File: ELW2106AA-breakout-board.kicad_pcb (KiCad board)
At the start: 2 copper layers, 77 x 18 mm, 28 parts, among them J1 Conn_02x04_Male-custom, U1 TLV61046ADB, U2 XC6206P332MR, U3 TXS0108EPW

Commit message: second revision
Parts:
- moved C10 11.6 mm to (117.9, 113.7), turned to 90 degrees
- moved L1 2.78 mm to (121.9, 103.2), turned to 0 degrees
- moved C4 1.86 mm to (137.4, 101.1), turned to 0 degrees
- moved R3 1.18 mm to (126.4, 101.2), turned to 180 degrees
- moved C7 0.92 mm to (140.9, 102.2), turned to -90 degrees
- moved R4 0.29 mm to (126.4, 103.7), turned to 0 degrees
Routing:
- net VCC: track 96.5 -> 55.1 mm, vias 2 -> 3
- net Net-(L1-Pad2): track 13.3 -> 5.12 mm
- net GND: track 13.8 -> 8.37 mm, vias 6 -> 33
- net +3V3: track 47.9 -> 43.7 mm
- net +16V: track 39.4 -> 42.8 mm, vias 2 -> 3
- net Net-(R3-Pad2): track 3.94 -> 5.46 mm
- net /OLED_CS: track 40.5 -> 41.7 mm
- net /OLED_RST: track 43.0 -> 44.1 mm
- net /OLED_D/C#: track 45.6 -> 46.6 mm
- net /OLED_SCLK: track 48.1 -> 49.0 mm
- net /OLED_MOSI: track 50.5 -> 51.3 mm
- added copper zone on B.Cu, net VCC

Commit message: third revision
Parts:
- C1, C10, C11, C12, C13, C2, C3, C4, C5, C6, C7, C8, C9, H1, J1, L1, R3, R4, TP1, TP2, TP3, TP4, TP5, TP6, TP7, U1, U2, U3: moved to F.Cu
- moved TP6 75.7 mm to (81.8, 102.0), turned to 0 degrees
- moved TP5 71.3 mm to (83.9, 102.0), turned to 0 degrees
- moved TP3 66.9 mm to (86.1, 102.0), turned to 0 degrees
- moved TP2 62.3 mm to (88.4, 102.0), turned to 0 degrees
- moved TP4 57.7 mm to (90.7, 102.0), turned to 0 degrees
- moved TP7 53.0 mm to (93.1, 102.0), turned to 0 degrees
- moved H1 47.9 mm to (95.6, 107.9)
- moved J1 47.5 mm to (143.3, 103.9), turned to 0 degrees
- moved TP1 43.3 mm to (97.9, 115.1), turned to 0 degrees
- moved C7 42.6 mm to (98.3, 102.2)
- moved C13 37.1 mm to (138.1, 102.9), turned to 0 degrees
- moved C6 36.4 mm to (101.4, 114.7), turned to 180 degrees
- moved C4 35.6 mm to (101.8, 101.0), turned to 180 degrees
- moved C1 31.9 mm to (103.6, 102.5), turned to 0 degrees
- moved C2 31.9 mm to (103.6, 103.9), turned to 0 degrees
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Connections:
- U3 pad 10: unconnected-(U3-Pad10) -> +3V3
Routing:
- net +3V3: track 43.7 -> 52.5 mm
- net GND: track 8.37 -> 7.89 mm, vias 33 -> 36
- added copper zone on F.Cu, net VCC
- removed copper zone on B.Cu, net VCC
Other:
- outline, holes or cut-outs redrawn
- board text added: "CS"
- board text added: "D/C"
- board text added: "ELW2106AA 4-wire SPI only"
- board text added: "GND"
- board text added: "MOSI"
- board text added: "RST"
- board text added: "SCLK"
- board text added: "VCC"

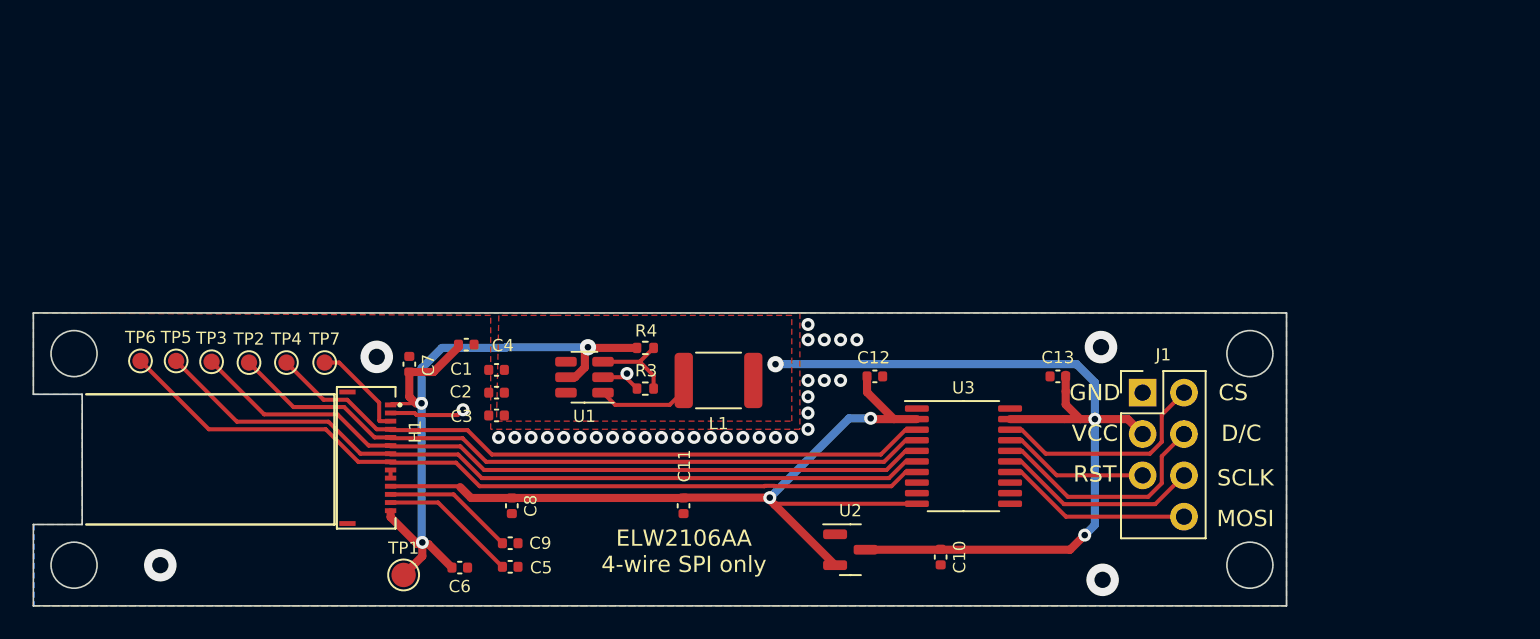
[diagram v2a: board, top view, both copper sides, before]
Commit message: replace TXS0108E with good ol' SN74LVC245
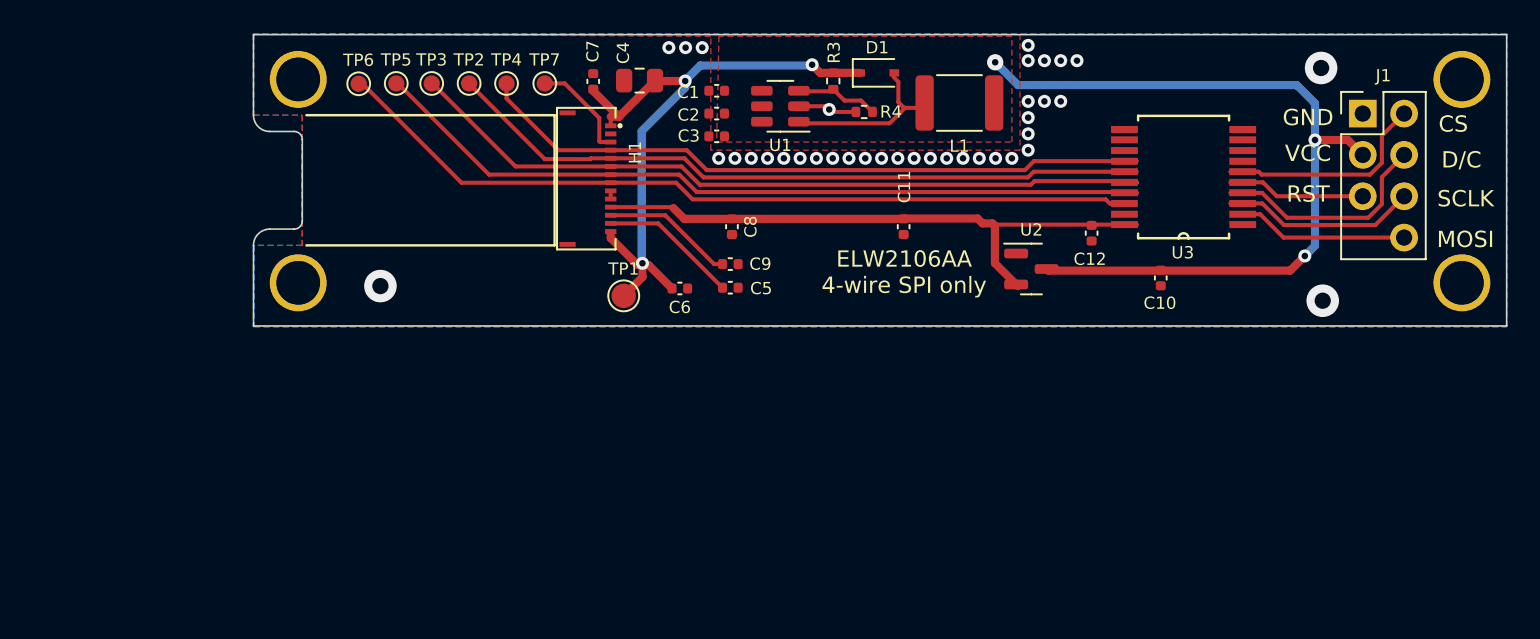
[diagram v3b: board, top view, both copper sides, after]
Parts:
- removed C13: 100nF, Capacitor_SMD:C_0402_1005Metric
- added D1: 1N5819WS, Diode_SMD:D_SOD-323, F.Cu at (127.0, 84.2)
- added MH1: MountingHole_Pad, custom:MountingHole_2.7mm_M2.5_Custom_Pad, B.Cu at (91.5, 97.2)
- added MH2: MountingHole_Pad, custom:MountingHole_2.7mm_M2.5_Custom_Pad, B.Cu at (91.5, 84.7)
- added MH3: MountingHole_Pad, custom:MountingHole_2.7mm_M2.5_Custom_Pad, B.Cu at (162.9, 97.2)
- added MH4: MountingHole_Pad, custom:MountingHole_2.7mm_M2.5_Custom_Pad, B.Cu at (162.9, 84.7)
- C10, C11: value 10uF -> 1µF
- C4: value 10µF -> 22µF; footprint Capacitor_SMD:C_0402_1005Metric -> Capacitor_SMD:C_0805_2012Metric
- C8, C9: value 1.0µF -> 1µF
- L1: value 12µH -> 22µH
- U1: value TLV61046ADB -> MT3608
- U3: value TXS0108EPW -> SN74LVC245ADBRG4; footprint Package_SO:TSSOP-20_4.4x6.5mm_P0.65mm -> SN74LVC245ADBRG4:SOP65P780X200-20N
- moved L1 22.6 mm to (132.1, 86.1)
- moved C6 21.8 mm to (114.9, 97.5)
- moved C9 21.8 mm to (118.0, 96.0)
- moved H1 21.8 mm to (109.2, 90.8)
- moved J1 21.8 mm to (156.9, 86.8)
- moved C11 21.8 mm to (128.7, 93.7)
- moved C5 21.8 mm to (118.0, 97.5)
- moved TP1 21.8 mm to (111.5, 98.0)
- moved TP2 21.8 mm to (102.0, 84.9)
- moved TP4 21.8 mm to (104.2, 84.9)
- moved U3 21.8 mm to (145.8, 90.7), turned to 180 degrees
- moved C1 21.8 mm to (117.2, 85.3)
- moved C2 21.8 mm to (117.2, 86.8)
- moved C10 21.8 mm to (144.4, 96.8)
- moved C3 21.8 mm to (117.2, 88.2)
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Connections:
- U1 pad 5: +16V -> VCC
- U1 pad 6: VCC -> unconnected-(U1-Pad6)
- U3 pad 1: unconnected-(U3-Pad1) -> GND
- U3 pad 10: +3V3 -> GND
- U3 pad 12: unconnected-(U3-Pad12) -> GND
- U3 pad 13: unconnected-(U3-Pad13) -> GND
- U3 pad 14: /MOSI -> /OLED_CS
- U3 pad 15: /SCLK -> /OLED_RST
- U3 pad 16: /D/C -> /OLED_D/C#
- U3 pad 17: /RESET -> /OLED_SCLK
- U3 pad 18: /CS -> /OLED_MOSI
- U3 pad 19: VCC -> GND
- U3 pad 2: +3V3 -> /MOSI
- U3 pad 20: unconnected-(U3-Pad20) -> +3V3
- U3 pad 3: /OLED_CS -> /SCLK
- U3 pad 4: /OLED_RST -> /D/C
- U3 pad 5: /OLED_D/C# -> /RESET
- U3 pad 6: /OLED_SCLK -> /CS
- U3 pad 7: /OLED_MOSI -> GND
- U3 pad 8: unconnected-(U3-Pad8) -> GND
- U3 pad 9: unconnected-(U3-Pad9) -> GND
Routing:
- net +3V3: track 52.5 -> 37.1 mm, vias 2 -> 0
- net VCC: track 55.2 -> 49.9 mm
- net Net-(D1-Pad2): track 5.12 -> 10.1 mm
- net GND: track 7.89 -> 3.76 mm, vias 36 -> 37
- net +16V: track 42.9 -> 39.7 mm
- net /MOSI: track 11.8 -> 10.5 mm
- net /OLED_MOSI: track 51.3 -> 50.0 mm
- net /SCLK: track 12.5 -> 12.0 mm
- net /RESET: track 9.04 -> 8.49 mm
- net /CS: track 13.8 -> 13.3 mm
- net /D/C: track 14.4 -> 13.9 mm
- net /OLED_RST: track 44.1 -> 43.6 mm
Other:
- board size 77 x 18 mm -> 77 x 17.9 mm
- board text added: "0.2000 mm / 0.0000 mm"
- board text added: "0.3000 mm"
- board text added: "1.6000 mm"
- board text added: "2"
- board text added: "77.1000 mm x 18.1000 mm"
- board text added: "BOARD CHARACTERISTICS"
- board text added: "Board Thickness:"
- board text added: "Board overall dimensions:"
- board text added: "Castellated pads:"
- board text added: "Copper Finish:"
- board text added: "Copper Layer Count:"
- board text added: "Edge card connectors:"
- board text added: "Impedance Control:"
- board text added: "Min hole diameter:"
- board text added: "Min track/spacing:"
- board text added: "No"
- board text added: "None"
- board text added: "Plated Board Edge:"

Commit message: final draft, add jlcpcb information for fabbing/assembly
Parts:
- H1: footprint ELW2106AA:MOLEX_503480-1400 -> Various:AFC24-S14FIA-00
- MH1, MH2, MH3, MH4: footprint custom:MountingHole_2.7mm_M2.5_Custom_Pad -> custom:MountingHole_2.2mm_M2_Custom_Pad
- U3: footprint SN74LVC245ADBRG4:SOP65P780X200-20N -> SN74LVC245APWR:SOP65P640X120-20N
- moved C3 18.7 mm to (135.6, 85.3), turned to 180 degrees
- moved C1 18.6 mm to (135.6, 88.1), turned to 180 degrees
- moved C2 18.4 mm to (135.6, 86.7), turned to 180 degrees
- moved R4 5.42 mm to (121.5, 83.9)
- moved D1 2.21 mm to (126.2, 86.3)
- moved C4 1.88 mm to (114.2, 84.1), turned to 180 degrees
- moved C7 1.46 mm to (110.7, 83.8), turned to 0 degrees
- moved TP7 1.26 mm to (106.5, 83.6)
- moved TP2 1.25 mm to (102.0, 83.6)
- moved TP3 1.25 mm to (99.7, 83.6)
- moved TP4 1.25 mm to (104.2, 83.6)
- moved TP5 1.25 mm to (97.5, 83.6)
- moved TP6 1.25 mm to (95.2, 83.7)
- moved R3 1.03 mm to (124.9, 83.9), turned to 180 degrees
- moved L1 0.98 mm to (131.1, 86.0)
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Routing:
- net +16V: track 39.7 -> 46.5 mm
- net /FRAME_SYNC: track 6.38 -> 8.11 mm
- net GND: track 3.76 -> 5.28 mm, vias 37 -> 33
- net /OLED_RST: track 43.6 -> 44.9 mm
- net /OLED_CS: track 41.7 -> 43.0 mm
- net VCC: track 49.9 -> 48.7 mm
- net /OLED_MOSI: track 50.0 -> 51.2 mm
- net Net-(D1-Pad2): track 10.1 -> 9.12 mm
- net Net-(R3-Pad2): track 5.19 -> 4.59 mm
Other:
- board text added: "77.1000 mm x 18.0000 mm"
- board text removed: "77.1000 mm x 18.1000 mm"
